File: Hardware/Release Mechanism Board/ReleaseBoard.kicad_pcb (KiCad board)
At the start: 2 copper layers, 77 x 30 mm, 43 parts, among them J1 CONN_01X02, J2 CONN_01X02, J3 CONN_02X03, J4 CONN_02X04, J5 CONN_01X02, J6 CONN_01X02, J7 CONN_01X02, Q1 Q_NMOS_GDS, Q2 Q_NMOS_GDS, U1 LM7809CT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

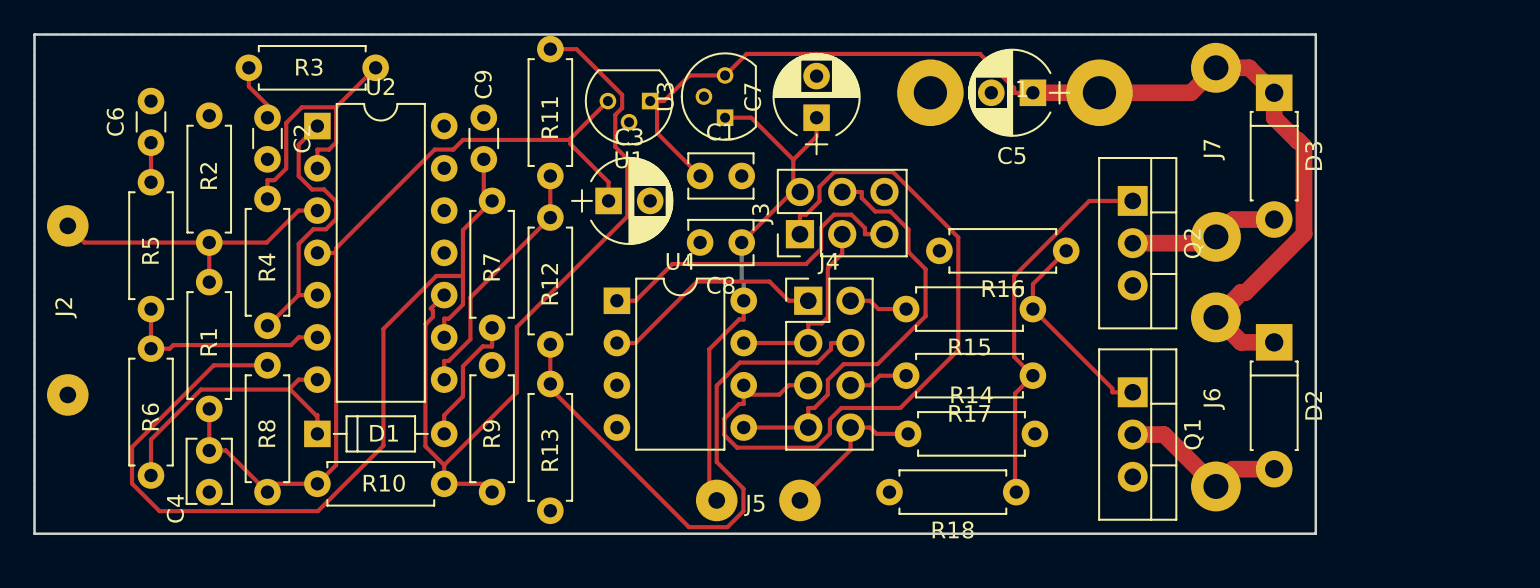
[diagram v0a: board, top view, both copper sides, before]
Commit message: -Release mechanism board updated with new peak detector design -Changes to release mechansim board PCB made -Added small version of Avalon logo -Regenerated release mechansim board gerber and drill files
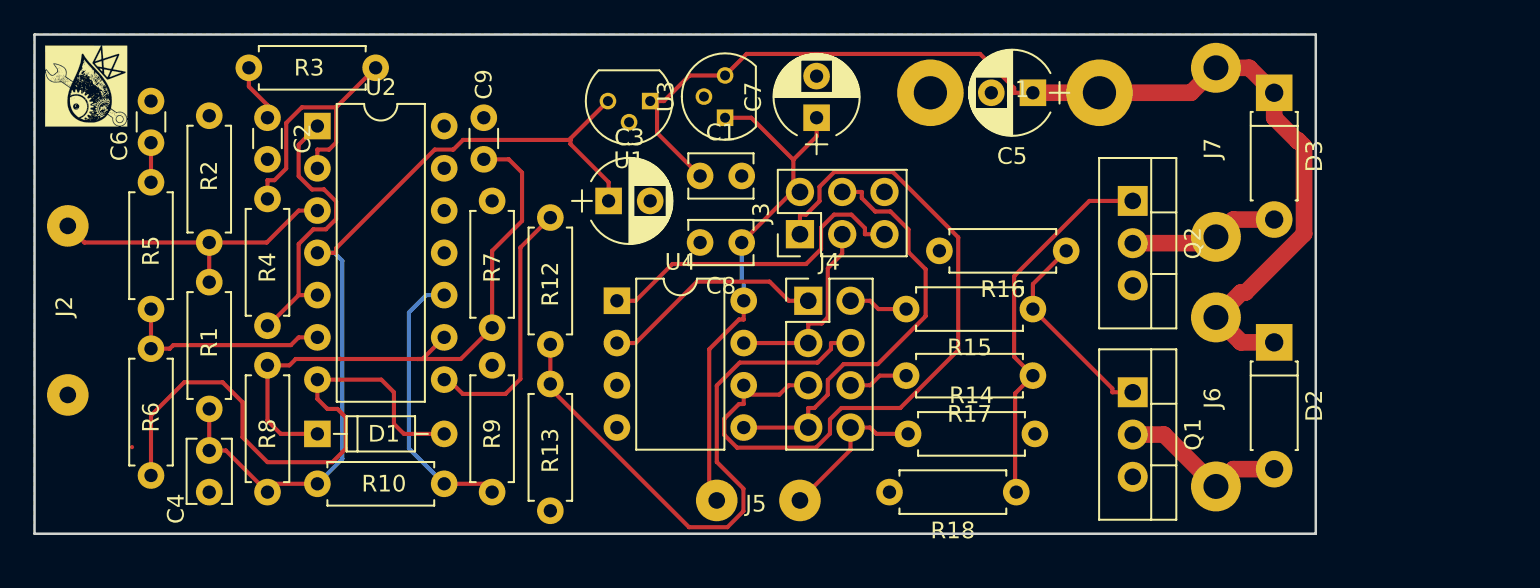
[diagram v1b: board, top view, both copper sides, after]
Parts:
- removed R11: 4.7M, Resistors_ThroughHole:R_Axial_DIN0207_L6.3mm_D2.5mm_P7.62mm_Horizontal
- added G***: LOGO, Footprints:Avalon Logo Small Footprint, F.Cu at (64.1, 124.1)
- C9: value 100n -> 10n
- R12: value R -> 8k
- R13: value R -> 10k
- R7: value 4.7M -> 10k
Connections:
- D1 pad 1: Net-(D1-Pad1) -> Net-(C9-Pad1)
- R6 pad 1: Net-(D1-Pad1) -> Net-(D1-Pad2)
- R7 pad 1: Net-(C9-Pad1) -> GND
- R7 pad 2: Net-(D1-Pad2) -> Net-(C9-Pad1)
- U2 pad 7: Net-(D1-Pad1) -> Net-(D1-Pad2)
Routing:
- net Net-(R10-Pad2): track 48.2 -> 16.8 mm
- net Net-(D1-Pad2): track 7.90 -> 35.0 mm
- net Net-(C9-Pad1): track 55.2 -> 35.9 mm
- net Net-(D1-Pad1): track 17.1 -> 0.00 mm
- net Net-(C3-Pad1): track 50.7 -> 52.0 mm
- net Net-(R12-Pad1): track 15.0 -> 16.1 mm
- net GND: track 0.00 -> 0.71 mm
- removed copper zone on F.Cu, net (none)
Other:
- net class Default: clearance 0.3 -> 0.2
- rule trace_clearance: 0.3 -> 0.2

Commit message: -Updated release mecahnsim board with fuse
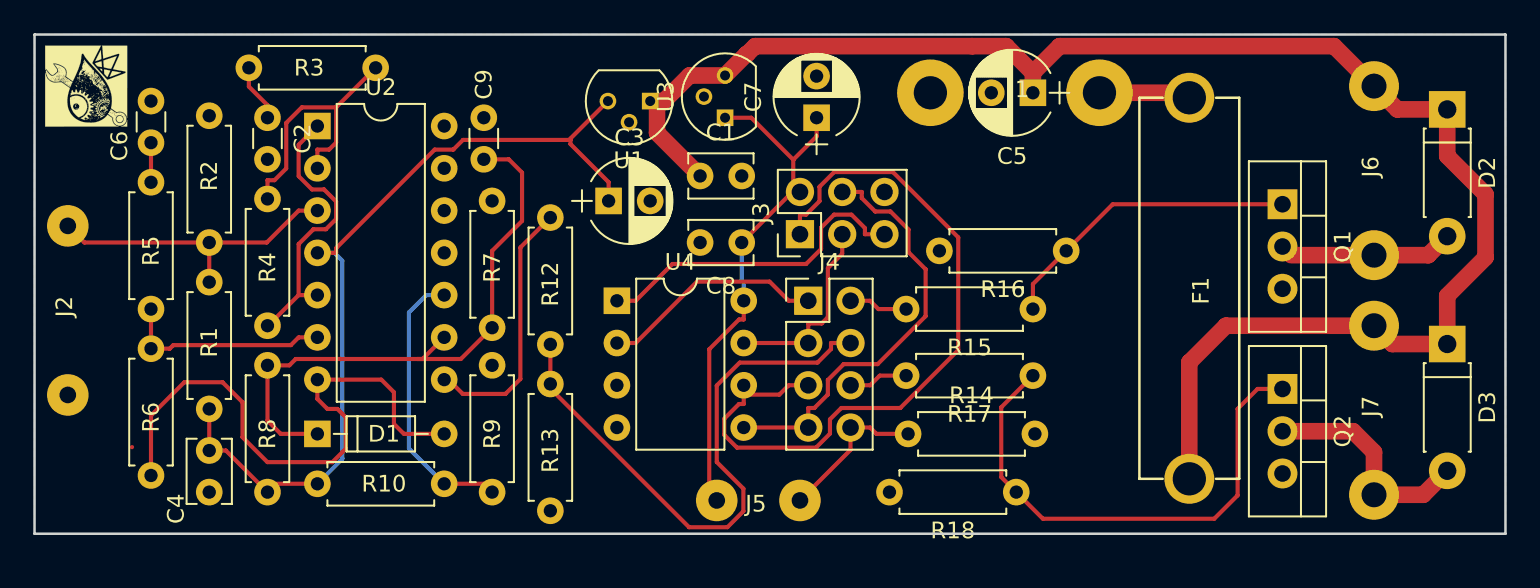
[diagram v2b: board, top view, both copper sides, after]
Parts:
- added F1: Fuse, Footprints:Keystone20x5FuseHolder, F.Cu at (130.4, 124.8)
- moved D3 18.3 mm to (145.9, 139.6)
- moved J7 18.2 mm to (141.5, 138.5)
- moved D2 17.4 mm to (145.9, 125.5)
- moved J6 16.8 mm to (141.5, 124.1)
- moved Q1 14.4 mm to (136.0, 131.2)
- moved Q2 14.4 mm to (136.0, 142.3)
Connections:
- J1 pad 1: +12V -> Net-(F1-Pad2)
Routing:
- net +12V: track 84.1 -> 98.8 mm
- net Net-(Q2-Pad1): track 22.9 -> 31.2 mm
- net Net-(Q1-Pad1): track 12.5 -> 18.5 mm
- net Net-(F1-Pad2): track 0.00 -> 5.52 mm
- net Net-(D3-Pad2): track 9.09 -> 13.6 mm
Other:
- board size 77 x 30 mm -> 88.4 x 30 mm

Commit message: -Updated release mechanism board with condensed design -Updated release mechanism board gerber files
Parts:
- moved Q1 12.2 mm to (123.8, 131.1)
- moved Q2 12.1 mm to (123.9, 142.1)
- moved D3 10.7 mm to (135.3, 140.9)
- moved D2 10.5 mm to (135.4, 125.4)
- moved R13 9.83 mm to (98.9, 149.0), turned to 180 degrees
- moved R12 6.40 mm to (92.0, 138.4)
- moved J6 6.33 mm to (135.4, 122.4)
- moved U1 3.41 mm to (95.1, 126.8)
- moved C3 3.31 mm to (92.6, 132.6)
- moved J7 3.26 mm to (138.3, 139.1)
- moved C8 3.04 mm to (100.5, 133.0)
- moved R16 3.01 mm to (120.0, 134.3)
- moved C1 3.01 mm to (98.0, 129.3)
- moved J3 2.93 mm to (104.1, 132.6)
- moved R15 1.20 mm to (120.1, 138.3)
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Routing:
- net Net-(J3-Pad1): track 45.7 -> 13.4 mm
- net Net-(Q2-Pad1): track 31.2 -> 11.1 mm
- net +5V: track 31.7 -> 45.7 mm
- net Net-(D1-Pad2): track 35.0 -> 24.8 mm
- net Net-(C3-Pad1): track 52.0 -> 62.2 mm
- net Net-(Q1-Pad1): track 18.5 -> 9.53 mm
- net Net-(R12-Pad1): track 16.1 -> 7.76 mm
- net Net-(R10-Pad2): track 16.8 -> 24.8 mm
- net Net-(J4-Pad4): track 35.6 -> 30.2 mm
- net Net-(D2-Pad2): track 10.6 -> 15.5 mm
- net Net-(D3-Pad2): track 13.6 -> 17.5 mm
- net Net-(C9-Pad1): track 35.9 -> 32.1 mm
- net Net-(R3-Pad1): track 16.6 -> 13.5 mm
- net Net-(J3-Pad5): track 19.7 -> 16.9 mm
- net Net-(J3-Pad4): track 25.7 -> 27.2 mm
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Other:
- board size 88.4 x 30 mm -> 80 x 30 mm
